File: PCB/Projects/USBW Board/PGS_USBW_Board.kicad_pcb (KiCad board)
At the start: 4 copper layers, 50.8 x 32.6 mm, 47 parts, among them IC1 BQ27621YZFR-G1A, J1 Molex 505110-1792, J2 USB4056-03-A, J4 PH 2.0 JST, P1 RPI-RM2, Q1 BSS138DW, Q2 BSS138DW, U1 USBLC6-2P6, U2 USBLC6-2P6, U3 USBLC6-2P6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

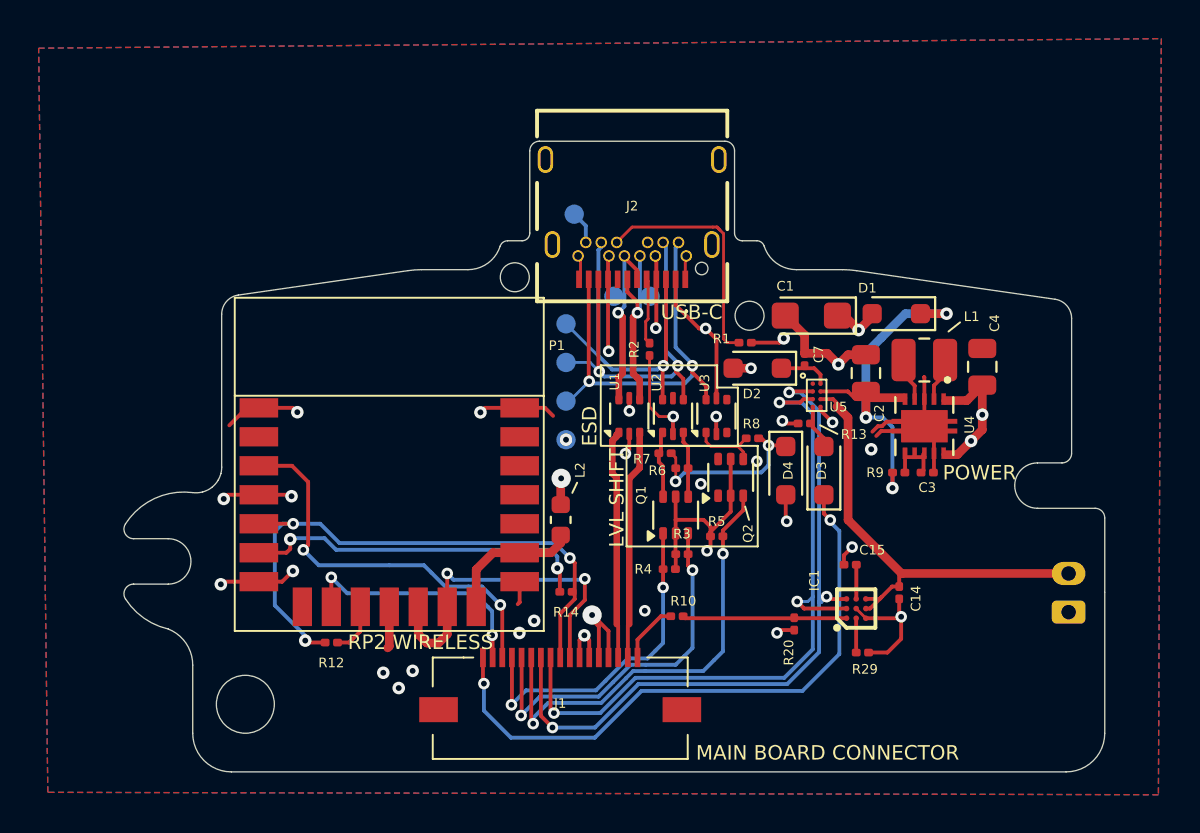
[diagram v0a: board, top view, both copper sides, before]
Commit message: Main Board/Trigger Board Update
- Main board updated with Kailh tactile switches
- Trigger board updated with Kailh tactile switches
- USBW board updated to remove unneeded diode, move position of USB-C port
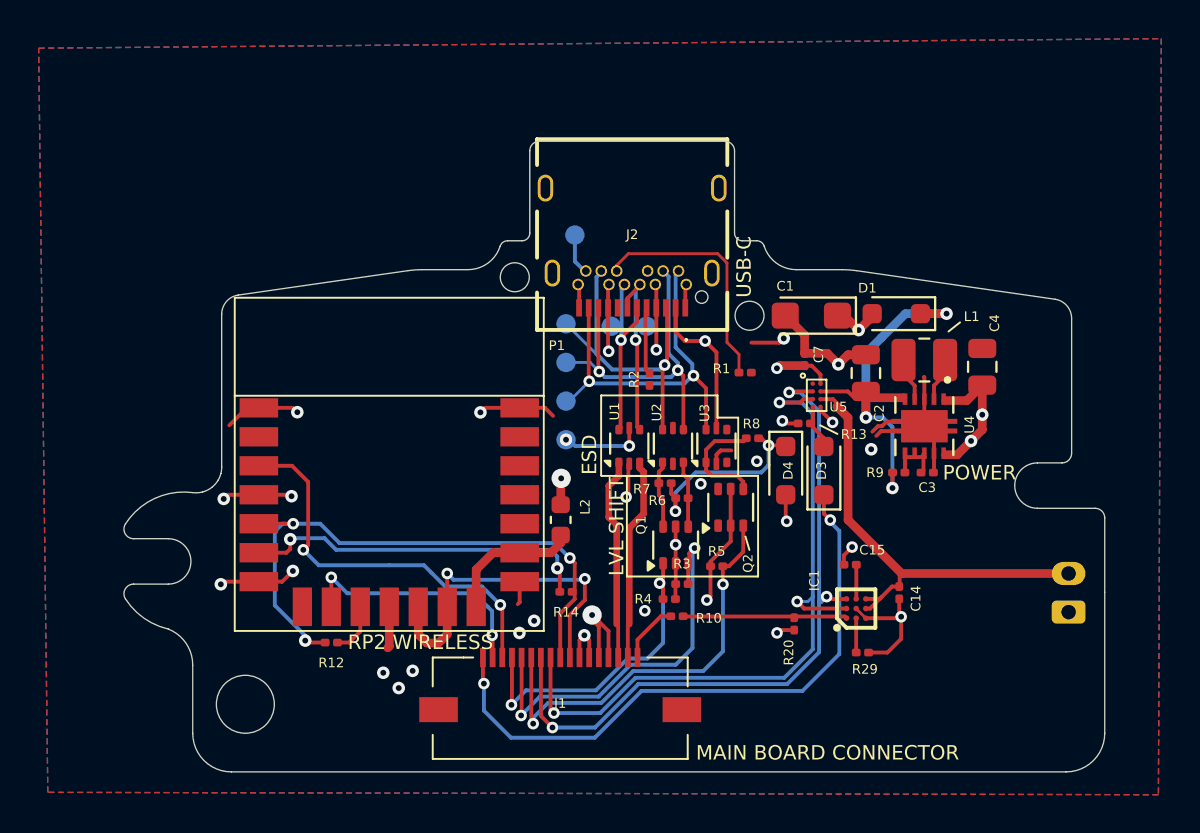
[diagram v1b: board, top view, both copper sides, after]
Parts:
- removed D2: CUS08F30,H3F, Diode_SMD:D_SOD-323_HandSoldering
- moved TP4 1.56 mm to (67.8, 27.1)
- moved TP5 1.56 mm to (66.0, 27.1)
- moved Q1 1.55 mm to (69.3, 38.5)
- moved R5 1.55 mm to (71.5, 39.6)
- moved R1 1.55 mm to (72.9, 29.6)
- moved R2 1.55 mm to (68.0, 29.9)
- moved U1 1.55 mm to (66.9, 33.4)
- moved U2 1.55 mm to (69.2, 33.4)
- moved U3 1.55 mm to (71.4, 33.4)
- moved Q2 1.55 mm to (72.2, 36.5)
- moved R3 1.55 mm to (69.7, 40.5)
- moved R4 1.55 mm to (69.0, 41.3)
- moved R6 1.55 mm to (69.7, 36.0)
- moved R7 1.55 mm to (68.8, 35.3)
- moved J2 1.48 mm to (67.1, 20.0)
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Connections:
- J2 pad A4: VBUS_PRE -> VBUS
- J2 pad A9: VBUS_PRE -> VBUS
- J2 pad B4: VBUS_PRE -> VBUS
- J2 pad B9: VBUS_PRE -> VBUS
- TP7 pad 1: VBUS_PRE -> VBUS
- U1 pad 5: VBUS_PRE -> VBUS
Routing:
- net VBUS: track 2.63 -> 32.6 mm, vias 0 -> 5
- net VBUS_PRE: track 27.8 -> 0.00 mm, vias 5 -> 0
- net GND: track 59.4 -> 55.7 mm, vias 25 -> 23
- net N_DATA_SAFE: track 3.60 -> 5.93 mm
- net N_DATA: track 21.8 -> 19.8 mm
- net N_LATCH: track 19.8 -> 18.1 mm
- net SAFE_D+: track 11.9 -> 10.5 mm
- net SAFE_D-: track 11.9 -> 10.5 mm
- net N_DATA_3.3: track 23.5 -> 22.1 mm
- net N_CLOCK: track 18.4 -> 17.1 mm
- net +3V3: track 26.9 -> 25.7 mm, vias 7 -> 8
- net SHARED_PU: track 9.32 -> 10.5 mm
- net N_LATCH_3.3: track 19.4 -> 20.6 mm
- net D+: track 9.24 -> 10.1 mm

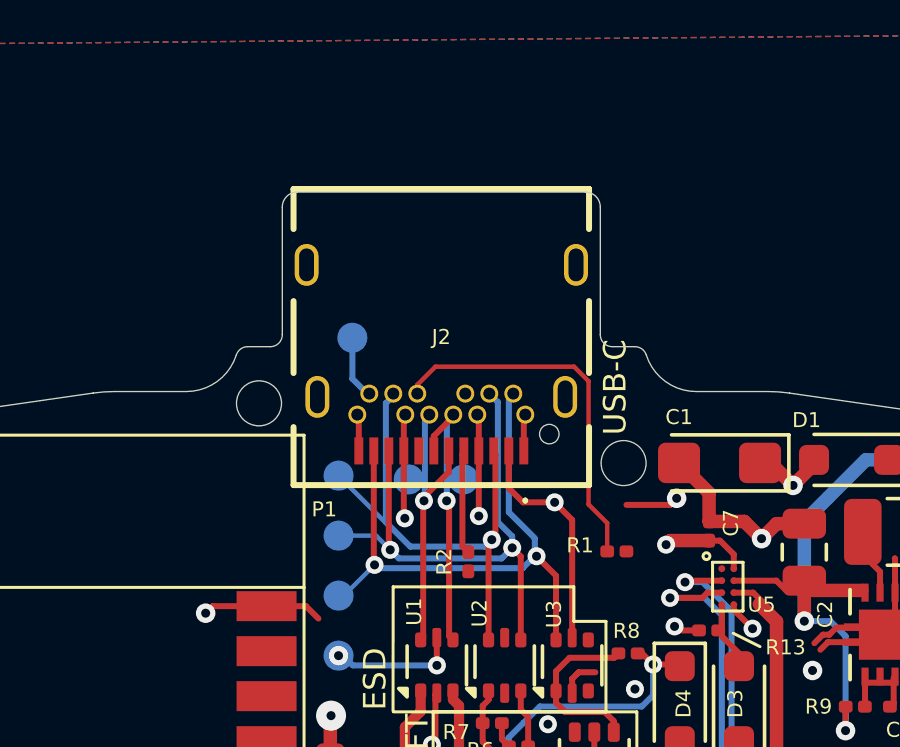
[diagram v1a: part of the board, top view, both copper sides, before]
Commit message: USB C Port Adjustment
- Spacing between USB C port and USB C cable adjusted
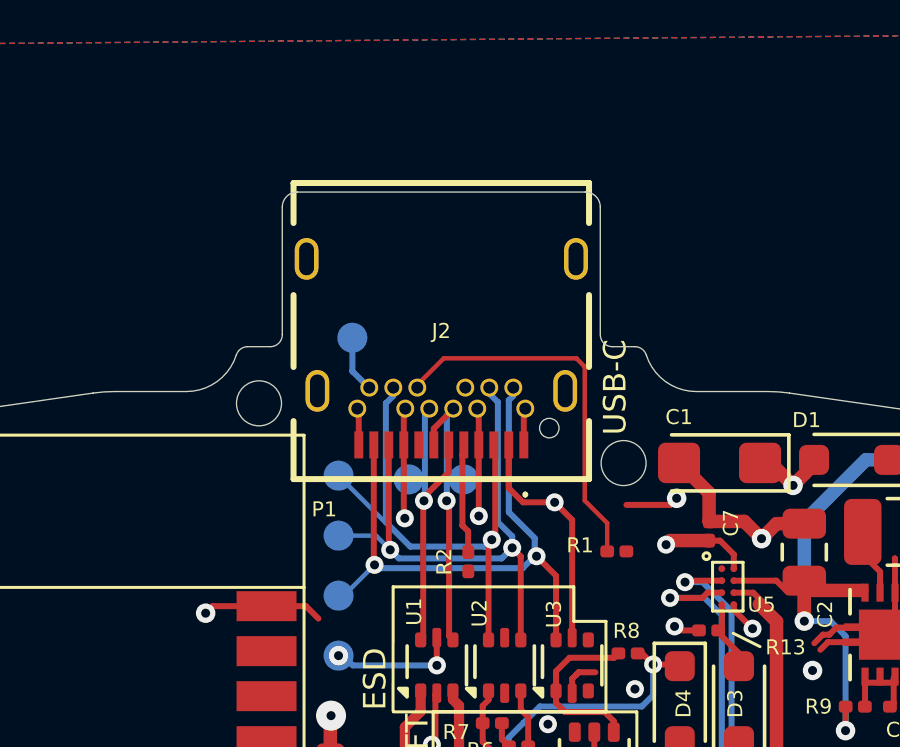
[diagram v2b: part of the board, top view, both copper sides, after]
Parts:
- moved J2 0.20 mm to (67.1, 19.8)

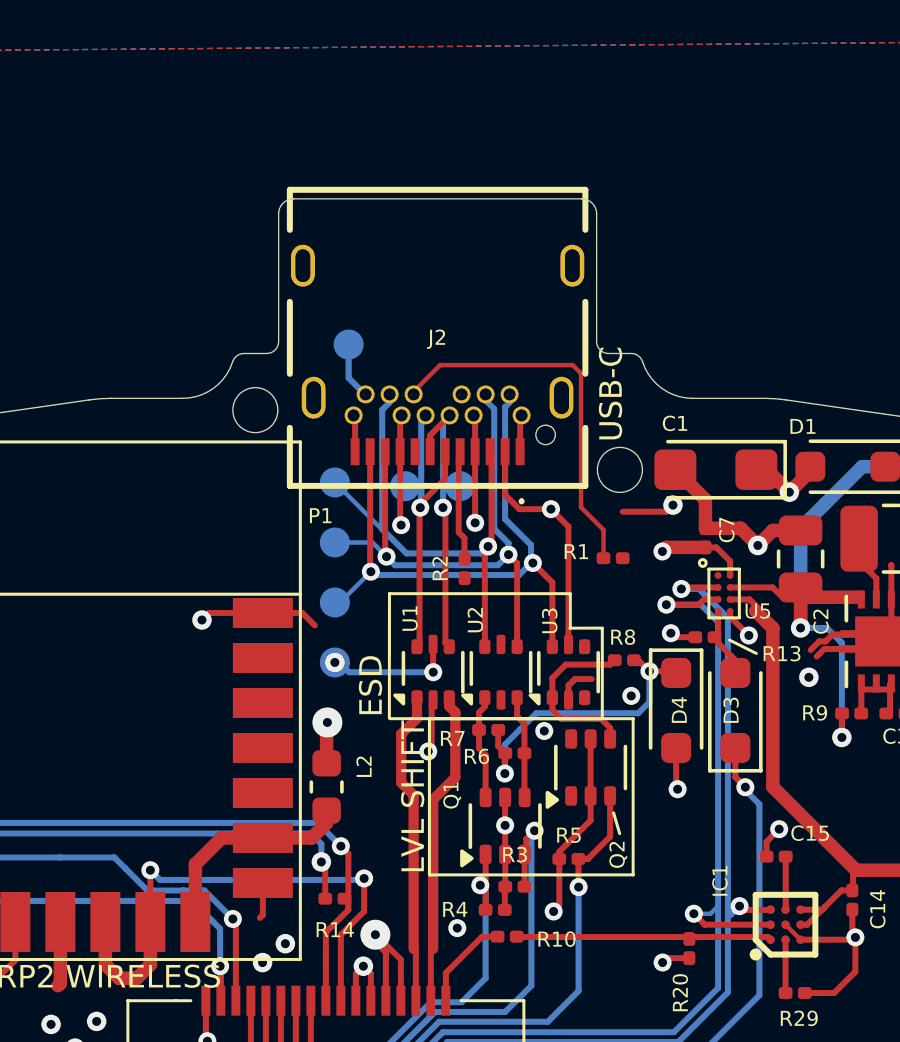
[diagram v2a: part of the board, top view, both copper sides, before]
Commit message: USB-C Adjustment
Adjusted USB-C port to have 0.3mm clearance between shell and overmold on the USB-C cable
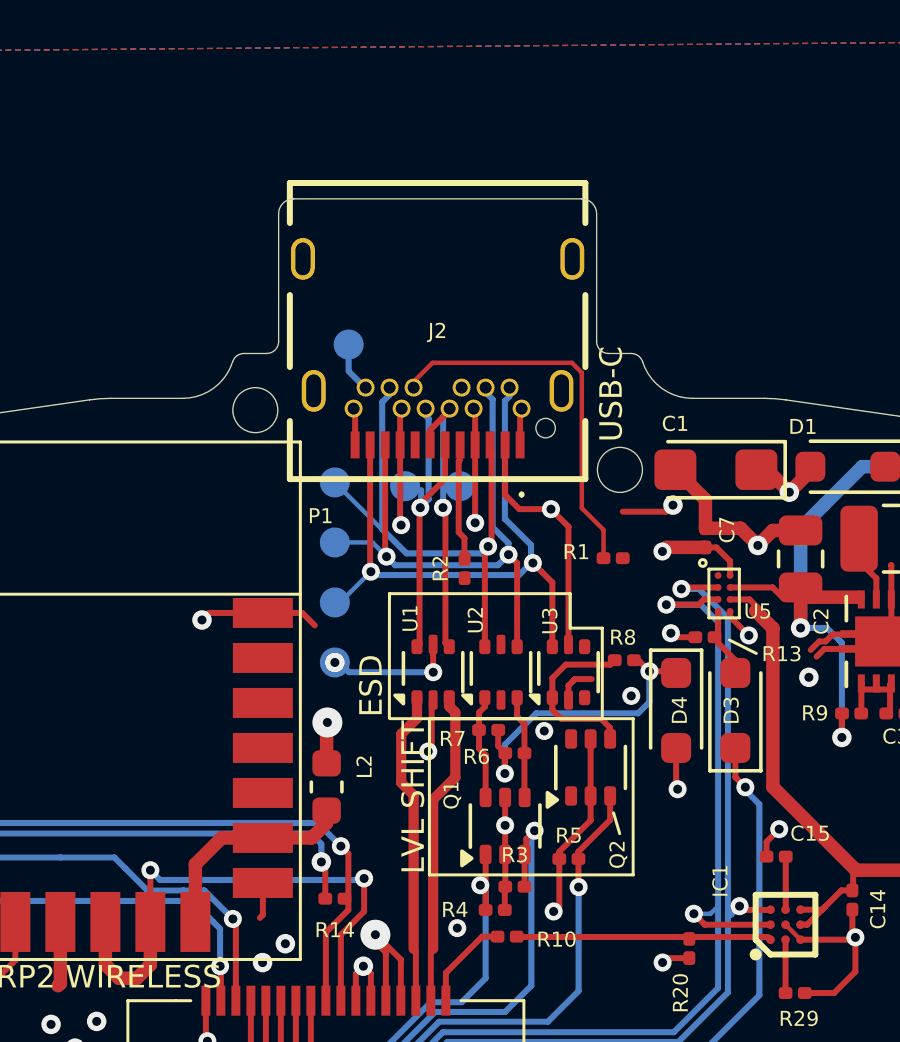
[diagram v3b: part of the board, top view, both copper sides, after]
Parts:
- moved J2 0.23 mm to (67.1, 19.6)
